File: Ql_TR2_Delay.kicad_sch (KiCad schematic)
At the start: 20 parts, among them U1 74HC86, U2 74HC04, U3 74HC04, U4 74HC04, U5 74HC04

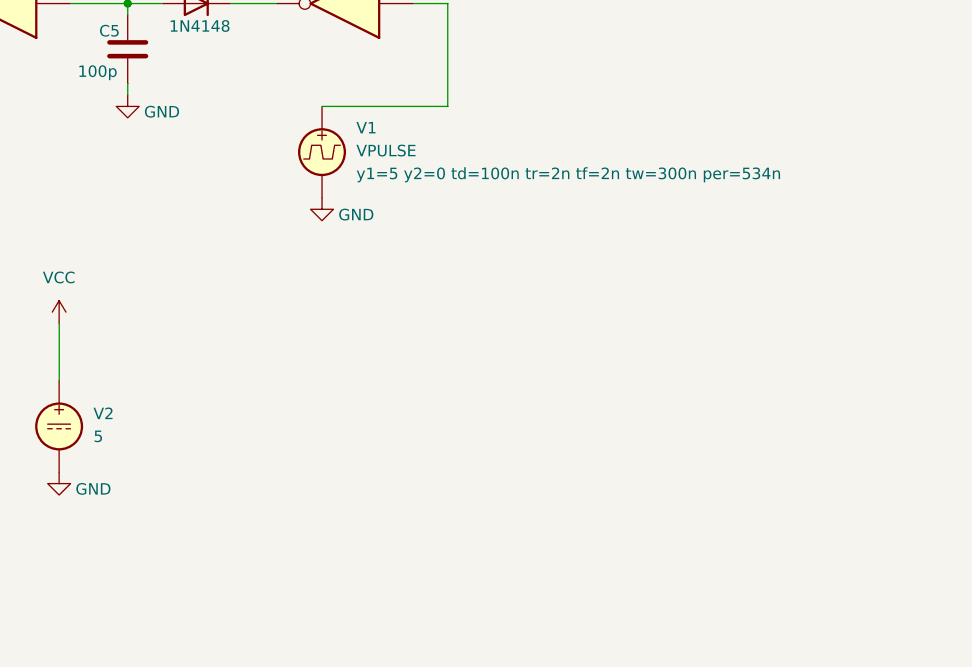
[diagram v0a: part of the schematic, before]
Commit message: Añadido CLK
CLK 7.5MHz
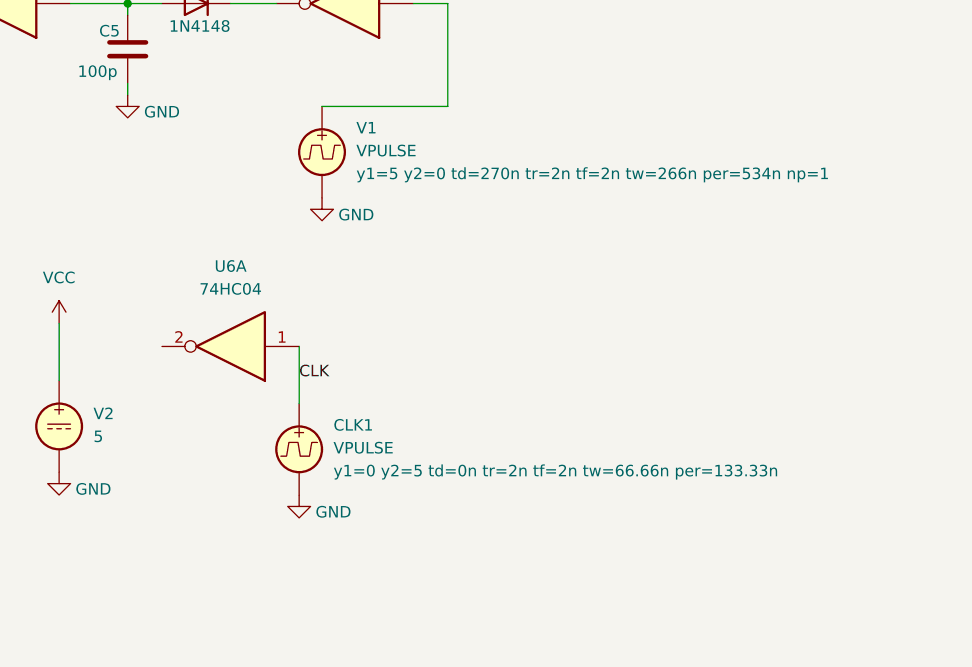
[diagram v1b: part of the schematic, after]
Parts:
- added CLK1: VPULSE, symbol Simulation_SPICE:VPULSE
- added U6: 74HC04, symbol 74xx:74HC04
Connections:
- net GND: now also CLK1.2
- new net CLK: CLK1.1, U6.1
